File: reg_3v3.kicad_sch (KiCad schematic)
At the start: 11 parts

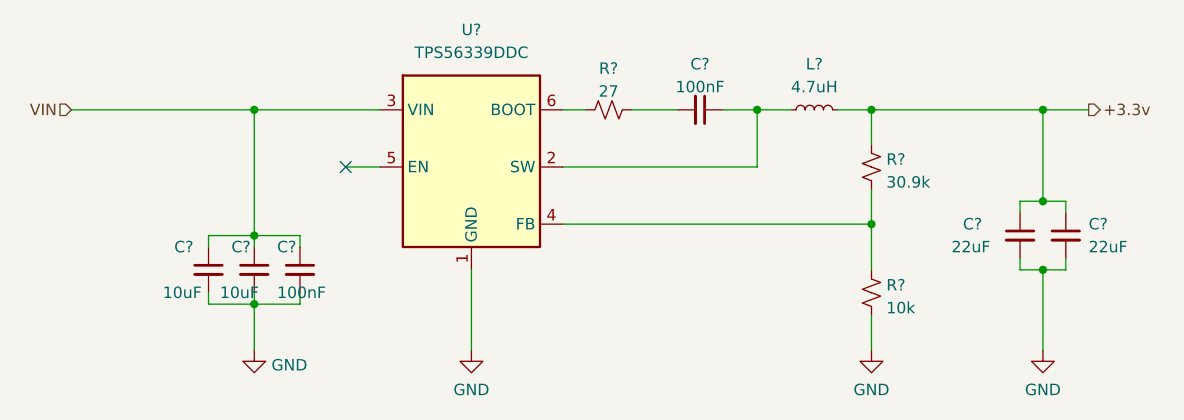
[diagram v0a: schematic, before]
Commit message: Finish schematic and start routing PCB
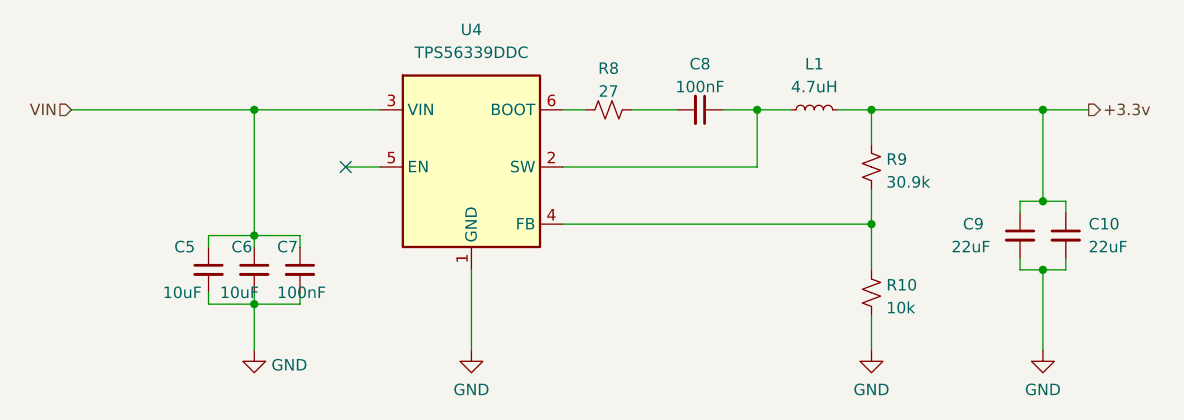
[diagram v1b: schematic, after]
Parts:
- C10, C5, C6, C7, C8, C9: renamed from C?; footprint (none) -> Capacitor_SMD:C_0805_2012Metric_Pad1.18x1.45mm_HandSolder
- L1: renamed from L?; footprint (none) -> Inductor_SMD:L_0805_2012Metric_Pad1.15x1.40mm_HandSolder
- R10, R8, R9: renamed from R?; footprint (none) -> Resistor_SMD:R_0805_2012Metric_Pad1.20x1.40mm_HandSolder
- gave numbers to parts that had none: 1
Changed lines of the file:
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@@
   (symbol (lib_id "Device:C_Small") (at 109.22 43.18 270) (unit 1)
     (in_bom yes) (on_board yes)
-    (property "Reference" "C?" (id 0) (at 109.22 38.1 90))
+    (property "Reference" "C8" (id 0) (at 109.22 38.1 90))
     (property "Value" "100nF" (id 1) (at 109.22 40.64 90))
-    (property "Footprint" "" (id 2) (at 109.22 43.18 0)
+    (property "Footprint" "Capacitor_SMD:C_0805_2012Metric_Pad1.18x1.45mm_HandSolder" (id 2) (at 109.22 43.18 0)
       (effects (font (size 1.27 1.27)) hide)
     )
@@
   (symbol (lib_id "Device:R_Small_US") (at 128.27 49.53 0) (unit 1)
     (in_bom yes) (on_board yes) (fields_autoplaced)
-    (property "Reference" "R?" (id 0) (at 129.921 48.6953 0)
+    (property "Reference" "R9" (id 0) (at 129.921 48.6953 0)
       (effects (font (size 1.27 1.27)) (justify left))
     )
@@
       (effects (font (size 1.27 1.27)) (justify left))
     )
-    (property "Footprint" "" (id 2) (at 128.27 49.53 0)
+    (property "Footprint" "Resistor_SMD:R_0805_2012Metric_Pad1.20x1.40mm_HandSolder" (id 2) (at 128.27 49.53 0)
       (effects (font (size 1.27 1.27)) hide)
     )
@@
   (symbol (lib_id "power:GND") (at 128.27 69.85 0) (unit 1)
     (in_bom yes) (on_board yes) (fields_autoplaced)
-    (property "Reference" "#PWR?" (id 0) (at 128.27 76.2 0)
+    (property "Reference" "#PWR032" (id 0) (at 128.27 76.2 0)
       (effects (font (size 1.27 1.27)) hide)
     )
@@
   (symbol (lib_id "Device:C_Small") (at 54.61 60.96 0) (unit 1)
     (in_bom yes) (on_board yes)
-    (property "Reference" "C?" (id 0) (at 50.8 58.42 0)
+    (property "Reference" "C5" (id 0) (at 50.8 58.42 0)
       (effects (font (size 1.27 1.27)) (justify left))
     )
@@
       (effects (font (size 1.27 1.27)) (justify left))
     )
-    (property "Footprint" "" (id 2) (at 54.61 60.96 0)
+    (property "Footprint" "Capacitor_SMD:C_0805_2012Metric_Pad1.18x1.45mm_HandSolder" (id 2) (at 54.61 60.96 0)
       (effects (font (size 1.27 1.27)) hide)
     )
@@
   (symbol (lib_id "Device:R_Small_US") (at 128.27 63.5 0) (unit 1)
     (in_bom yes) (on_board yes) (fields_autoplaced)
-    (property "Reference" "R?" (id 0) (at 129.921 62.6653 0)
+    (property "Reference" "R10" (id 0) (at 129.921 62.6653 0)
       (effects (font (size 1.27 1.27)) (justify left))
     )
@@
       (effects (font (size 1.27 1.27)) (justify left))
     )
-    (property "Footprint" "" (id 2) (at 128.27 63.5 0)
+    (property "Footprint" "Resistor_SMD:R_0805_2012Metric_Pad1.20x1.40mm_HandSolder" (id 2) (at 128.27 63.5 0)
       (effects (font (size 1.27 1.27)) hide)
     )
@@
   (symbol (lib_id "power:GND") (at 83.82 69.85 0) (unit 1)
     (in_bom yes) (on_board yes) (fields_autoplaced)
-    (property "Reference" "#PWR?" (id 0) (at 83.82 76.2 0)
+    (property "Reference" "#PWR031" (id 0) (at 83.82 76.2 0)
       (effects (font (size 1.27 1.27)) hide)
     )
@@
   (symbol (lib_id "power:GND") (at 59.69 69.85 0) (mirror y) (unit 1)
     (in_bom yes) (on_board yes) (fields_autoplaced)
-    (property "Reference" "#PWR?" (id 0) (at 59.69 76.2 0)
+    (property "Reference" "#PWR030" (id 0) (at 59.69 76.2 0)
       (effects (font (size 1.27 1.27)) hide)
     )
@@
   (symbol (lib_id "Regulator_Switching:TPS56339DDC") (at 83.82 53.34 0) (unit 1)
     (in_bom yes) (on_board yes)
-    (property "Reference" "U?" (id 0) (at 83.82 34.29 0))
+    (property "Reference" "U4" (id 0) (at 83.82 34.29 0))
     (property "Value" "TPS56339DDC" (id 1) (at 83.82 36.83 0))
     (property "Footprint" "Package_TO_SOT_SMD:SOT-23-6" (id 2) (at 85.09 59.69 0)
@@
   (symbol (lib_id "Device:R_Small_US") (at 99.06 43.18 270) (unit 1)
     (in_bom yes) (on_board yes) (fields_autoplaced)
-    (property "Reference" "R?" (id 0) (at 99.06 38.5912 90))
+    (property "Reference" "R8" (id 0) (at 99.06 38.5912 90))
     (property "Value" "27" (id 1) (at 99.06 41.1281 90))
-    (property "Footprint" "" (id 2) (at 99.06 43.18 0)
+    (property "Footprint" "Resistor_SMD:R_0805_2012Metric_Pad1.20x1.40mm_HandSolder" (id 2) (at 99.06 43.18 0)
       (effects (font (size 1.27 1.27)) hide)
     )
@@
   (symbol (lib_id "Device:C_Small") (at 59.69 60.96 0) (unit 1)
     (in_bom yes) (on_board yes)
-    (property "Reference" "C?" (id 0) (at 57.15 58.42 0)
+    (property "Reference" "C6" (id 0) (at 57.15 58.42 0)
       (effects (font (size 1.27 1.27)) (justify left))
     )
@@
       (effects (font (size 1.27 1.27)) (justify left))
     )
-    (property "Footprint" "" (id 2) (at 59.69 60.96 0)
+    (property "Footprint" "Capacitor_SMD:C_0805_2012Metric_Pad1.18x1.45mm_HandSolder" (id 2) (at 59.69 60.96 0)
       (effects (font (size 1.27 1.27)) hide)
     )
@@
   (symbol (lib_id "Device:C_Small") (at 149.86 57.15 0) (unit 1)
     (in_bom yes) (on_board yes)
-    (property "Reference" "C?" (id 0) (at 152.4 55.88 0)
+    (property "Reference" "C10" (id 0) (at 152.4 55.88 0)
       (effects (font (size 1.27 1.27)) (justify left))
     )
@@
       (effects (font (size 1.27 1.27)) (justify left))
     )
-    (property "Footprint" "" (id 2) (at 149.86 57.15 0)
+    (property "Footprint" "Capacitor_SMD:C_0805_2012Metric_Pad1.18x1.45mm_HandSolder" (id 2) (at 149.86 57.15 0)
       (effects (font (size 1.27 1.27)) hide)
     )
@@
   (symbol (lib_id "Device:C_Small") (at 144.78 57.15 0) (unit 1)
     (in_bom yes) (on_board yes)
-    (property "Reference" "C?" (id 0) (at 138.43 55.88 0)
+    (property "Reference" "C9" (id 0) (at 138.43 55.88 0)
       (effects (font (size 1.27 1.27)) (justify left))
     )
@@
       (effects (font (size 1.27 1.27)) (justify left))
     )
-    (property "Footprint" "" (id 2) (at 144.78 57.15 0)
+    (property "Footprint" "Capacitor_SMD:C_0805_2012Metric_Pad1.18x1.45mm_HandSolder" (id 2) (at 144.78 57.15 0)
       (effects (font (size 1.27 1.27)) hide)
     )
@@
   (symbol (lib_id "power:GND") (at 147.32 69.85 0) (unit 1)
     (in_bom yes) (on_board yes) (fields_autoplaced)
-    (property "Reference" "#PWR?" (id 0) (at 147.32 76.2 0)
+    (property "Reference" "#PWR033" (id 0) (at 147.32 76.2 0)
       (effects (font (size 1.27 1.27)) hide)
     )
@@
   (symbol (lib_id "Device:L_Small") (at 121.92 43.18 90) (unit 1)
     (in_bom yes) (on_board yes)
-    (property "Reference" "L?" (id 0) (at 121.92 38.1 90))
+    (property "Reference" "L1" (id 0) (at 121.92 38.1 90))
     (property "Value" "4.7uH" (id 1) (at 121.92 40.64 90))
-    (property "Footprint" "" (id 2) (at 121.92 43.18 0)
+    (property "Footprint" "Inductor_SMD:L_0805_2012Metric_Pad1.15x1.40mm_HandSolder" (id 2) (at 121.92 43.18 0)
       (effects (font (size 1.27 1.27)) hide)
     )
@@
   (symbol (lib_id "Device:C_Small") (at 64.77 60.96 0) (unit 1)
     (in_bom yes) (on_board yes)
-    (property "Reference" "C?" (id 0) (at 62.23 58.42 0)
+    (property "Reference" "C7" (id 0) (at 62.23 58.42 0)
       (effects (font (size 1.27 1.27)) (justify left))
     )
@@
       (effects (font (size 1.27 1.27)) (justify left))
     )
-    (property "Footprint" "" (id 2) (at 64.77 60.96 0)
-      (effects (font (size 1.27 1.27)) hide)
-    )
+    (property "Footprint" "Capacitor_SMD:C_0805_2012Metric_Pad1.18x1.45mm_HandSolder" (id 2) (at 64.77 60.96 0)
+      (effects (font (size 1.27 1.27)) hide)
+    )
